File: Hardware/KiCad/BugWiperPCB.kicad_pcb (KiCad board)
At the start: 2 copper layers, 121.9 x 50.8 mm, 18 parts, among them J1 UJ20-C-H-G-SMT-1-P16-TR, U1 ESP32-S3-WROOM-1, U2 IFX007TAUMA1, U3 IFX007TAUMA1, U5 WE-TVS-82400102

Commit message: KiCad Motor part
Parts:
- added C10: 68n, Capacitor_SMD:C_0603_1608Metric, F.Cu at (193.4, 50.0)
- added C11: 220p, Capacitor_SMD:C_0603_1608Metric, F.Cu at (193.4, 52.5)
- added C12: 220p, Capacitor_SMD:C_0603_1608Metric, F.Cu at (193.4, 55.0)
- added C5: 68n, Capacitor_SMD:C_0603_1608Metric, F.Cu at (189.3, 50.0)
- added C6: C, Capacitor_SMD:C_0603_1608Metric, F.Cu at (189.3, 52.5)
- added C7: 68n, Capacitor_SMD:C_0603_1608Metric, F.Cu at (189.3, 55.0)
- added C8: C, Capacitor_SMD:C_0603_1608Metric, F.Cu at (189.3, 57.5)
- added C9: 68n, Capacitor_SMD:C_0603_1608Metric, F.Cu at (189.3, 60.0)
- added JP1: SolderJumper_3_Bridged12, Jumper:SolderJumper-3_P1.3mm_Open_RoundedPad1.0x1.5mm, F.Cu at (190.2, 63.1)
- added R10: 4k7, Resistor_SMD:R_0603_1608Metric, F.Cu at (197.4, 52.5)
- added R11: 4k7, Resistor_SMD:R_0603_1608Metric, F.Cu at (197.4, 55.0)
- added R12: 1k2, Resistor_SMD:R_0603_1608Metric, F.Cu at (197.4, 57.5)
- added R7: 47k, Resistor_SMD:R_0603_1608Metric, F.Cu at (193.4, 57.5)
- added R8: 47k, Resistor_SMD:R_0603_1608Metric, F.Cu at (193.4, 60.0)
- added R9: 1k2, Resistor_SMD:R_0603_1608Metric, F.Cu at (197.4, 50.0)
- U2, U3: value IFX007TAUMA1 -> BTN70301EPAXUMA1_2; footprint BugWiper_lib:PG-TO263-7-1_INF -> BugWiper_lib:PG-TSDSO-14-22
- moved U2 17.4 mm to (182.9, 52.1)
- moved U3 6.07 mm to (182.9, 58.7)
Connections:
- U2 pad 2: unconnected-(U2-IN-Pad2) -> EN1
- U2 pad 3: unconnected-(U2-INH-Pad3) -> DEN1
- U2 pad 4: unconnected-(U2-OUT-Pad4) -> Net-(JP1-B)
- U2 pad 6: unconnected-(U2-IS-Pad6) -> IN1
- U2 pad 8: unconnected-(U2-OUT-Pad8) -> Motor+
- U3 pad 2: unconnected-(U3-IN-Pad2) -> EN2
- U3 pad 3: unconnected-(U3-INH-Pad3) -> DEN2
- U3 pad 4: unconnected-(U3-OUT-Pad4) -> Net-(JP1-C)
- U3 pad 6: unconnected-(U3-IS-Pad6) -> IN2
- U3 pad 8: unconnected-(U3-OUT-Pad8) -> Motor+

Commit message: update KiCAD files
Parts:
- added C13: 1nF, Capacitor_SMD:C_0603_1608Metric, F.Cu at (136.5, 66.7)
- added C14: 10nF, Capacitor_SMD:C_0603_1608Metric, F.Cu at (165.6, 74.9)
- added C15: 25uF, Capacitor_SMD:C_1210_3225Metric, F.Cu at (147.3, 33.0)
- added C16: 25uF, Capacitor_SMD:C_1210_3225Metric, F.Cu at (149.4, 72.4)
- added C17: 25uF, Capacitor_SMD:C_1210_3225Metric, F.Cu at (149.4, 66.7)
- added C18: 470uF, Capacitor_SMD:CP_Elec_8x10.5, F.Cu at (168.3, 86.4)
- added C19: 470uF, Capacitor_SMD:CP_Elec_8x10.5, F.Cu at (168.4, 95.9)
- added C20: 470uF, Capacitor_SMD:CP_Elec_8x10.5, F.Cu at (168.3, 105.4)
- added D3: D_TVS, Diode_SMD:D_SMB, F.Cu at (167.0, 48.9)
- added L1: IHLP4040DZER100M1A, BugWiper_lib:IND_IHLP-4040DZ_VIS, F.Cu at (159.4, 33.7)
- added Q1: NMOS_SO-8, BugWiper_lib:PowerPAK_SO-8L_3_VIS, F.Cu at (174.3, 40.2)
- added R13: 1k, Resistor_SMD:R_0603_1608Metric, F.Cu at (158.1, 59.7)
- added R14: 1k, Resistor_SMD:R_0603_1608Metric, F.Cu at (158.1, 61.6)
- added R15: 1k, Resistor_SMD:R_0603_1608Metric, F.Cu at (158.1, 63.5)
- added R16: 1k, Resistor_SMD:R_0603_1608Metric, F.Cu at (158.1, 54.0)
- added R17: 1k, Resistor_SMD:R_0603_1608Metric, F.Cu at (182.5, 50.2)
- added R18: 1k, Resistor_SMD:R_0603_1608Metric, F.Cu at (182.2, 65.8)
- added R19: 3k3, Resistor_SMD:R_0603_1608Metric, F.Cu at (138.4, 66.7)
- added R20: 22k, Resistor_SMD:R_0603_1608Metric, F.Cu at (138.4, 63.5)
- added R21: 1ok, Resistor_SMD:R_0603_1608Metric, F.Cu at (165.7, 71.8)
- added R22: 1k, Resistor_SMD:R_0603_1608Metric, F.Cu at (158.1, 55.9)
- added R23: 1k, Resistor_SMD:R_0603_1608Metric, F.Cu at (158.1, 57.8)
- added R24: 1k, Resistor_SMD:R_0603_1608Metric, F.Cu at (136.5, 63.5)
- C10, C7: value 68n -> 100uF; footprint Capacitor_SMD:C_0603_1608Metric -> Capacitor_SMD:C_1206_3216Metric
- C11, C12: value 220p -> 1nF
- C5, C9: value 68n -> 100nF
- R12, R9: value 1k2 -> 2k
- U2, U3: value BTN70301EPAXUMA1_2 -> BTN9960LV; footprint BugWiper_lib:PG-TSDSO-14-22 -> BugWiper_lib:IFX-PG-HSOF-7-1-V
- moved JP1 43.8 mm to (146.9, 56.2)
- moved C3 36.7 mm to (95.4, 42.5)
- moved R6 27.3 mm to (95.2, 60.3)
- moved C4 27.1 mm to (95.2, 62.2)
- moved U3 17.5 mm to (196.8, 69.2), turned to -90 degrees
- moved R11 17.1 mm to (184.2, 65.8), turned to 90 degrees
- moved C12 15.7 mm to (185.1, 68.4)
- moved C9 15.4 mm to (202.6, 67.9), turned to -90 degrees
- moved U2 14.5 mm to (196.8, 48.3), turned to 90 degrees
- moved R12 14.0 mm to (186.1, 65.8), turned to -90 degrees
- moved R8 13.6 mm to (204.5, 67.9), turned to 90 degrees
- moved C6 13.6 mm to (202.6, 49.5), turned to 90 degrees
- moved R10 13.1 mm to (184.4, 50.2), turned to 90 degrees
- moved C10 11.5 mm to (196.8, 61.0)
- moved R9 11.0 mm to (186.3, 50.2), turned to -90 degrees
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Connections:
- C11 pad 1: IN1 -> Net-(C11-Pad1)
- C12 pad 1: IN2 -> Net-(C12-Pad1)
- C8 pad 2: Motor+ -> Motor-
- C9 pad 1: Motor+ -> Motor-
- JP1 pad 1: Net-(JP1-A) -> /ESP32-S3/M_IHN2
- JP1 pad 3: Net-(JP1-B) -> /ESP32-S3/M_INH1
- R10 pad 1: IN1 -> Net-(C11-Pad1)
- R10 pad 2: Net-(JP1-B) -> Net-(U2-IS)
- R11 pad 1: IN2 -> Net-(C12-Pad1)
- R11 pad 2: Net-(JP1-A) -> Net-(U3-IS)
- R12 pad 1: Net-(JP1-A) -> Net-(U3-IS)
- R8 pad 1: Motor+ -> Motor-
- R9 pad 1: Net-(JP1-B) -> Net-(U2-IS)
- U2 pad 1: unconnected-(U2-NC-Pad1) -> GND
- U2 pad 2: EN1 -> GND
- U2 pad 3: DEN1 -> Net-(U2-IN)
- U2 pad 4: Net-(JP1-B) -> Net-(U2-INH)
- U2 pad 5: unconnected-(U2-NC-Pad5) -> Net-(U2-IS)
- U2 pad 6: IN1 -> +12V
- U2 pad 7: unconnected-(U2-NC-Pad7) -> +12V
- U3 pad 1: unconnected-(U3-NC-Pad1) -> GND
- U3 pad 2: EN2 -> GND
- U3 pad 3: DEN2 -> Net-(U3-IN)
- U3 pad 4: Net-(JP1-C) -> Net-(U3-INH)
- U3 pad 5: unconnected-(U3-NC-Pad5) -> Net-(U3-IS)
- U3 pad 6: IN2 -> +12V
- U3 pad 7: unconnected-(U3-NC-Pad7) -> +12V
- U3 pad 8: Motor+ -> Motor-

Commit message: Update PCB
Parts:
- added C21: 25uF, Capacitor_SMD:C_1210_3225Metric, F.Cu at (167.0, 45.4)
- added C22: 100nF, Capacitor_SMD:C_0603_1608Metric, F.Cu at (183.4, 54.5)
- added C23: 25uF, Capacitor_SMD:C_1210_3225Metric, F.Cu at (222.2, 57.8)
- added H1: MountingHole, MountingHole:MountingHole_3.2mm_M3_DIN965, F.Cu at (111.1, 25.4)
- added H2: MountingHole, MountingHole:MountingHole_3.2mm_M3_DIN965, F.Cu at (162.6, 25.4)
- added H3: MountingHole, MountingHole:MountingHole_3.2mm_M3_DIN965, F.Cu at (121.9, 68.6)
- added H4: MountingHole, MountingHole:MountingHole_3.2mm_M3_DIN965, F.Cu at (219.7, 25.4)
- added H5: MountingHole, MountingHole:MountingHole_3.2mm_M3_DIN965, F.Cu at (170.2, 69.2)
- added H6: MountingHole_Pad, MountingHole:MountingHole_3.2mm_M3_DIN965_Pad_TopBottom, F.Cu at (220.3, 68.6)
- added J2: TBLH10-350-06BK, TBLH10_350_06BK-2:CUI_TBLH10-350-06BK, F.Cu at (212.6, 31.6)
- added J3: Phoenix_1776508, BugWiper_lib:PHOENIX_1776508, F.Cu at (189.8, 20.5)
- added J4: RJ45, BugWiper_lib:CONN8_2-908LF_AMP, F.Cu at (152.4, 33.9)
- added R25: R004, Resistor_SMD:R_1206_3216Metric, F.Cu at (187.8, 58.1)
- added R26: 1k, Resistor_SMD:R_0603_1608Metric, F.Cu at (183.4, 53.0)
- added U4: INA180A2, Package_TO_SOT_SMD:SOT-23-5, F.Cu at (187.8, 54.3)
- R21: value 1ok -> 10k
- moved C18 51.6 mm to (212.1, 59.1), turned to 180 degrees
- moved S1 51.1 mm to (137.2, 21.0), turned to 180 degrees
- moved J1 48.9 mm to (128.6, 20.4), turned to 180 degrees
- moved C19 48.1 mm to (199.4, 59.1)
- moved S2 48.0 mm to (119.9, 20.9), turned to 180 degrees
- moved C20 45.7 mm to (167.6, 59.7)
- moved C4 44.3 mm to (119.5, 25.1), turned to -90 degrees
- moved R6 43.9 mm to (121.4, 25.1), turned to -90 degrees
- moved C3 43.7 mm to (135.9, 26.2), turned to -90 degrees
- moved R1 37.5 mm to (121.9, 28.1), turned to -90 degrees
- moved D1 34.2 mm to (133.3, 32.4), turned to 90 degrees
- moved R2 33.2 mm to (131.4, 32.4), turned to -90 degrees
- moved U5 32.0 mm to (128.6, 32.5), turned to -90 degrees
- moved R3 31.5 mm to (125.7, 32.4), turned to -90 degrees
- moved R7 29.1 mm to (217.2, 41.3), turned to 90 degrees
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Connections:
- C10 pad 1: +12V -> +12V_HighSide
- C19 pad 1: +12V -> +12V_HighSide
- C20 pad 1: +12V -> +12V_HighSide
- C6 pad 1: +12V -> +12V_HighSide
- C7 pad 1: +12V -> +12V_HighSide
- C8 pad 1: +12V -> +12V_HighSide
- U2 pad 6: +12V -> +12V_HighSide
- U2 pad 7: +12V -> +12V_HighSide
- U3 pad 6: +12V -> +12V_HighSide
- U3 pad 7: +12V -> +12V_HighSide
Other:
- board size 121.9 x 50.8 mm -> 117.5 x 52.1 mm

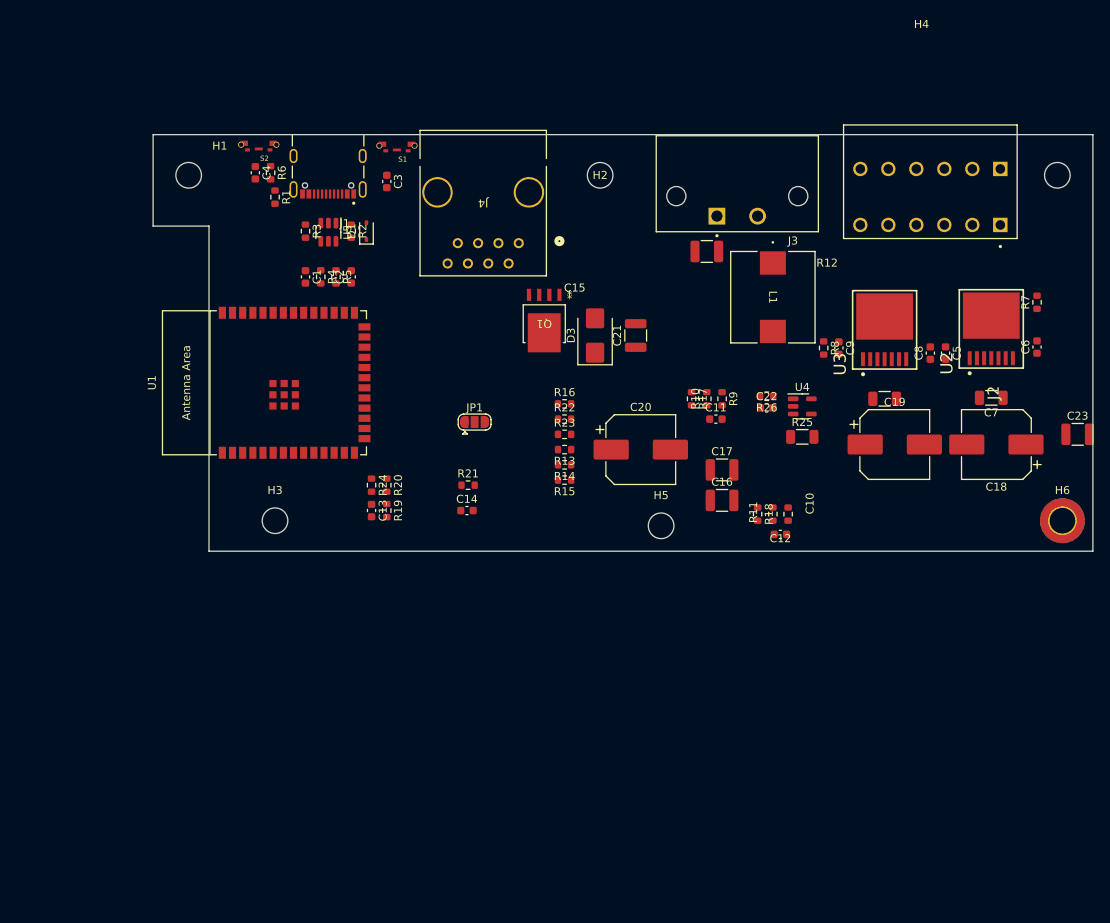
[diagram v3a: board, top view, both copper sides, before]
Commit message: update PCB
add 12V to 3.3V converter and 5V to 3.3V for USB
add protections to the RJ45
component placement
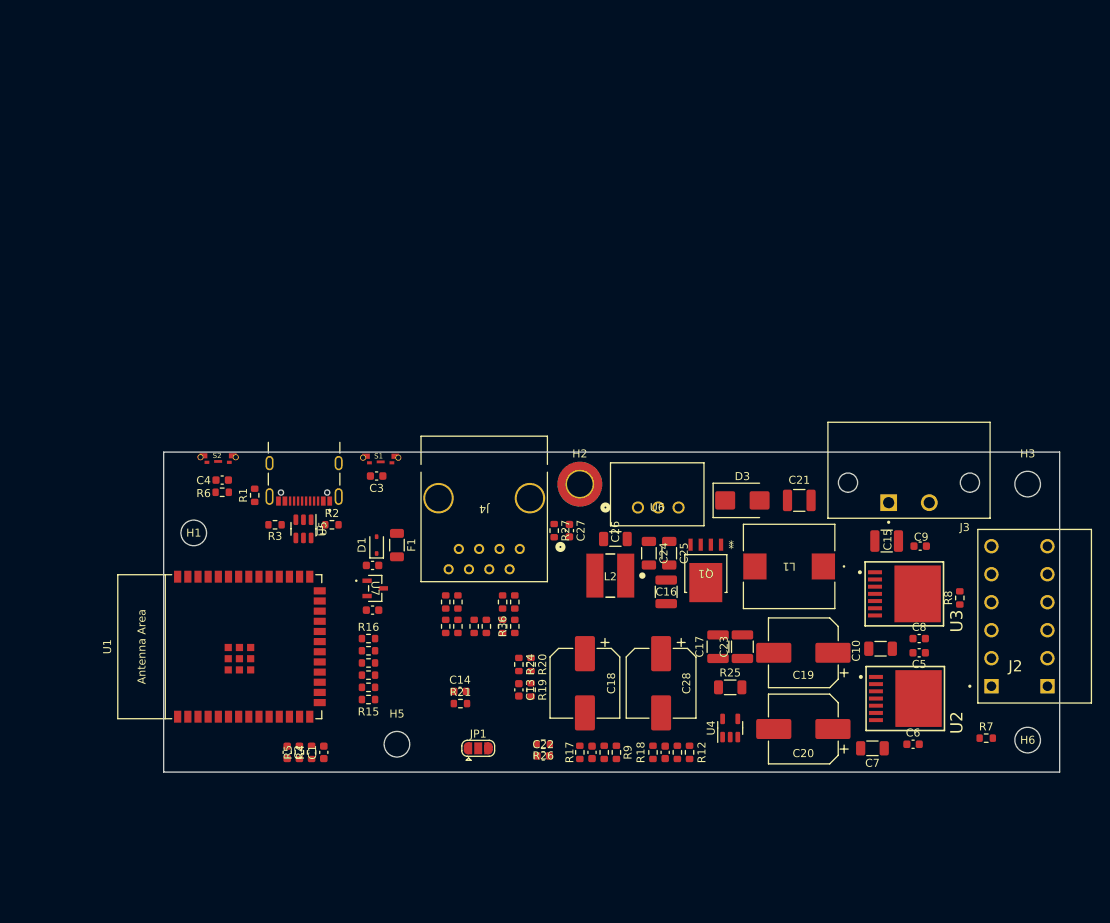
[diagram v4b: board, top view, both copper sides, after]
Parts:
- removed H4: MountingHole, MountingHole:MountingHole_3.2mm_M3_DIN965
- added C24: 4.7uF, Capacitor_SMD:C_1206_3216Metric, F.Cu at (168.7, 72.6)
- added C25: 4.7uF, Capacitor_SMD:C_1206_3216Metric, F.Cu at (171.2, 72.6)
- added C26: 4.7uF, Capacitor_SMD:C_1206_3216Metric, F.Cu at (164.5, 70.9)
- added C27: 100nF, Capacitor_SMD:C_0603_1608Metric, F.Cu at (158.7, 69.8)
- added C28: 470uF, Capacitor_SMD:CP_Elec_8x10.5, F.Cu at (170.2, 88.9)
- added C29: 100nF, Capacitor_SMD:C_0603_1608Metric, F.Cu at (134.1, 79.8)
- added C30: 100nF, Capacitor_SMD:C_0603_1608Metric, F.Cu at (134.1, 74.2)
- added F1: 100mA Polyfuse, Resistor_SMD:R_1206_3216Metric, F.Cu at (137.2, 71.6)
- added L2: 10µH 2.2A, BugWiper_lib:WE-PD2_5848, F.Cu at (163.8, 75.4)
- added R27: 1k, Resistor_SMD:R_0603_1608Metric, F.Cu at (156.8, 69.8)
- added R28: 1k, Resistor_SMD:R_0603_1608Metric, F.Cu at (151.9, 81.8)
- added R29: 1k, Resistor_SMD:R_0603_1608Metric, F.Cu at (150.4, 81.8)
- added R30: 5k, Resistor_SMD:R_0603_1608Metric, F.Cu at (151.9, 78.7)
- added R31: 5k, Resistor_SMD:R_0603_1608Metric, F.Cu at (150.4, 78.7)
- added R32: 1k, Resistor_SMD:R_0603_1608Metric, F.Cu at (143.3, 81.8)
- added R33: 5k, Resistor_SMD:R_0603_1608Metric, F.Cu at (143.3, 78.7)
- added R34: 1k, Resistor_SMD:R_0603_1608Metric, F.Cu at (144.8, 81.8)
- added R35: 5k, Resistor_SMD:R_0603_1608Metric, F.Cu at (144.8, 78.7)
- added R36: 330, Resistor_SMD:R_0603_1608Metric, F.Cu at (148.3, 81.8)
- added R37: 330, Resistor_SMD:R_0603_1608Metric, F.Cu at (146.8, 81.8)
- added U6: TSR 0.5-2433, BugWiper_lib:TSR0P5_TRP, F.Cu at (167.3, 66.9)
- added U7: AP7333-33SRG-7, BugWiper_lib:SOT23R_DIO, F.Cu at (134.4, 77.0)
- moved H3 94.2 mm to (216.0, 64.0)
- moved H6 88.5 mm to (216.0, 96.0)
- moved H2 60.5 mm to (160.0, 64.0)
- moved C2 60.0 mm to (123.4, 97.5), turned to -90 degrees
- moved R5 59.6 mm to (125.0, 97.5), turned to 90 degrees
- moved C1 59.5 mm to (128.0, 97.5), turned to 90 degrees
- moved C18 59.5 mm to (160.7, 88.9), turned to -90 degrees
- moved R4 59.4 mm to (126.5, 97.5), turned to 90 degrees
- moved J2 57.7 mm to (211.5, 89.3), turned to 90 degrees
- moved R7 54.9 mm to (210.8, 95.8), turned to 0 degrees
- moved C6 52.0 mm to (201.7, 96.5), turned to 0 degrees
- moved C22 51.7 mm to (155.4, 98.0)
- moved R26 51.7 mm to (155.4, 96.5)
- moved C23 49.6 mm to (180.3, 84.3), turned to 90 degrees
- moved U2 46.7 mm to (199.7, 90.8), turned to 0 degrees
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- renumbered H6 to H2, H2 to H6
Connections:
- J3 pad 1: GND -> /Power/+VBat
- J3 pad 2: /Power/+VBat -> GND
- J4 pad 1: unconnected-(J4-Pad1) -> GND
- J4 pad 2: unconnected-(J4-Pad2) -> Net-(J4-Pad2)
- J4 pad 3: unconnected-(J4-Pad3) -> Net-(J4-Pad3)
- J4 pad 4: unconnected-(J4-Pad4) -> Net-(J4-Pad4)
- J4 pad 5: unconnected-(J4-Pad5) -> Net-(J4-Pad5)
- J4 pad 6: unconnected-(J4-Pad6) -> Net-(J4-Pad6)
- J4 pad 7: unconnected-(J4-Pad7) -> Net-(J4-Pad7)
- J4 pad 8: unconnected-(J4-Pad8) -> Net-(F1-Pad2)
- R6 pad 2: +3V3 -> +3.3V
- U1 pad 2: +3V3 -> +3.3V
- U4 pad 5: +3V3 -> +3.3V
- U5 pad 5: +3V3 -> +3.3V
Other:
- board size 117.5 x 52.1 mm -> 112 x 40 mm

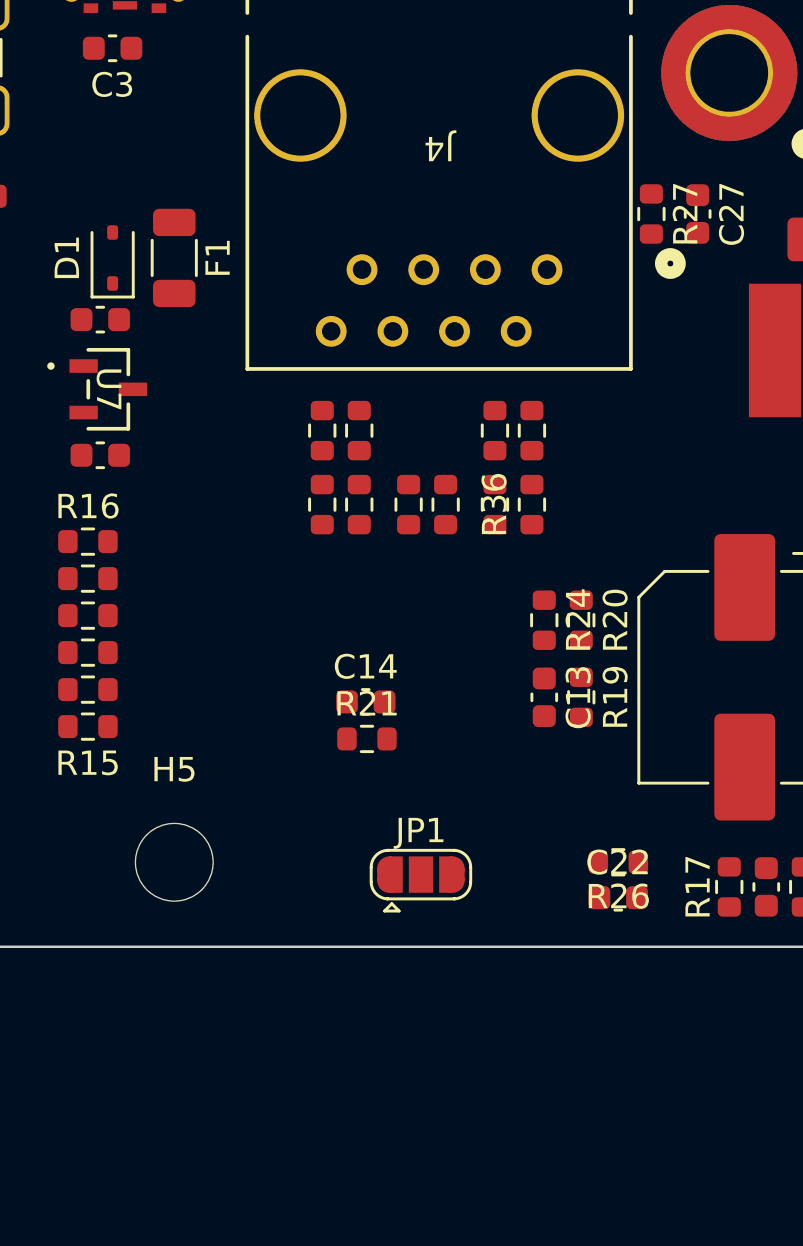
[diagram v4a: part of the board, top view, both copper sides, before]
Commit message: add ESD protection to inputs
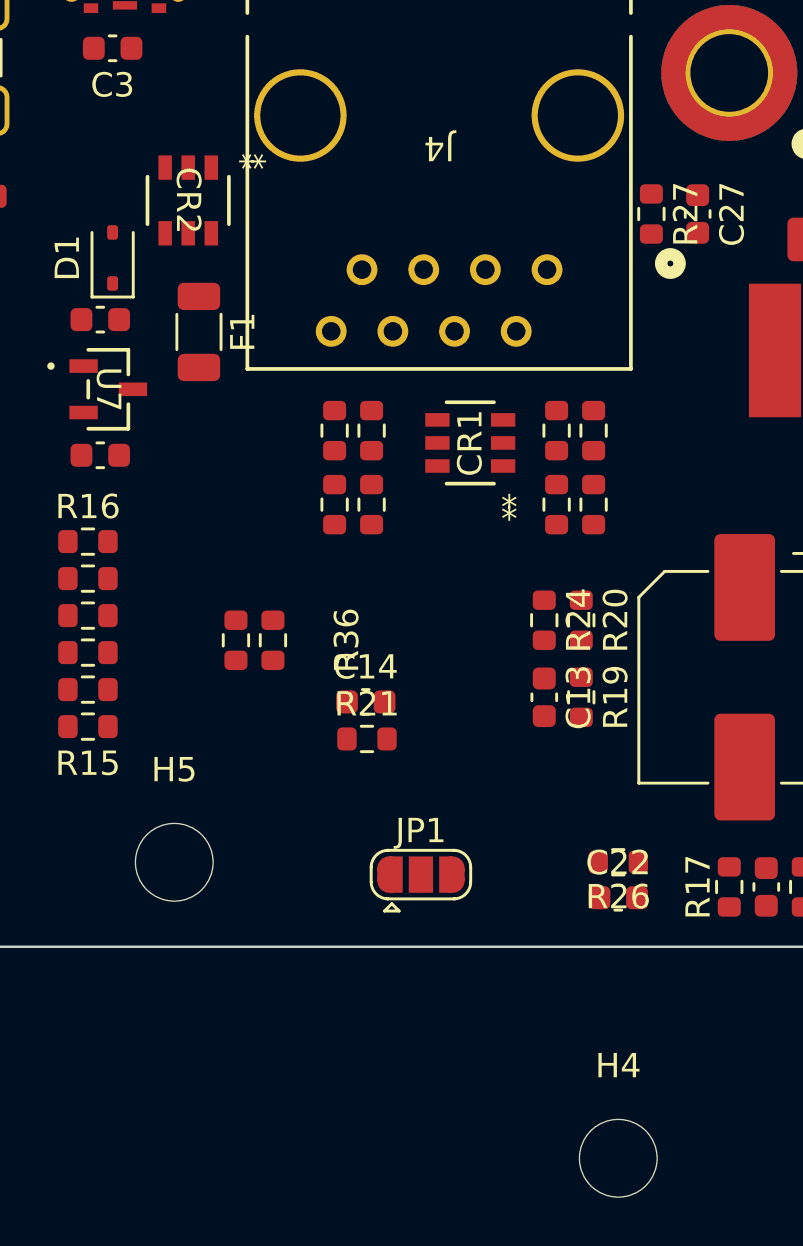
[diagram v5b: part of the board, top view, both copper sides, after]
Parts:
- added CR1: D5V0P4UR6SO-7, BugWiper_lib:SOT26_DIO, F.Cu at (149.4, 79.2)
- added CR2: D5V0P4UR6SO-7, BugWiper_lib:SOT26_DIO, F.Cu at (137.7, 69.3)
- added H4: MountingHole, MountingHole:MountingHole_3.2mm_M3_DIN965, F.Cu at (155.4, 108.7)
- R28, R32: value 1k -> 4k7
- moved R36 9.04 mm to (141.2, 87.4)
- moved R37 9.04 mm to (139.7, 87.4)
- moved F1 3.21 mm to (138.2, 74.7)
- moved R28 2.54 mm to (154.4, 81.8)
- moved R29 2.54 mm to (152.9, 81.8)
- moved R30 2.54 mm to (154.4, 78.7)
- moved R31 2.54 mm to (152.9, 78.7)
- moved R32 0.51 mm to (143.8, 81.8)
- moved R33 0.51 mm to (143.8, 78.7)
- moved R34 0.51 mm to (145.3, 81.8)
- moved R35 0.51 mm to (145.3, 78.7)
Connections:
- net Net-(J4-Pad4) renamed OUT_1
- net Net-(J4-Pad5) renamed OUT_2
- J2 pad 5_A: unconnected-(J2-5-Pad5_A) -> EN_C2
- J2 pad 6_A: unconnected-(J2-6-Pad6_A) -> EN_C1
- R22 pad 1: unconnected-(R22-Pad1) -> Enc1
- R23 pad 1: unconnected-(R23-Pad1) -> Enc2
